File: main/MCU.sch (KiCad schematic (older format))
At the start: 1 part

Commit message: Some cleanup
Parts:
- added C?: 1uF, symbol Device:C
- added C? (x3): 10nF, symbol Device:C
- added C? (x3): 10uF, symbol Device:C
- added C? (x7): 0.1uF, symbol Device:C
- added U?: EFM32GG990F1024, symbol energymicro-efm32:EFM32GG990F1024
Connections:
- new net: C?.1, C?.1, C?.1, C?.1, C?.1, C?.1, C?.1, C?.1, C?.1, U?.D5 (IOVDD_6), U?.F8 (VDD_DREG), U?.G4 (IOVDD_0), U?.K8 (AVDD_2), U?.K9 (AVDD_1), U?.L10 (AVDD_0)
- new net: C?.1, U?.D7 (IOVDD_5)
- new net: C?.1, U?.F11 (DECOUPLE)
- new net: C?.1, U?.G8 (IOVDD_4)
- new net: C?.1, U?.H7 (IOVDD_3)
- new net: C?.1, U?.L4 (IOVDD_1)
- new net GND: C?.2, C?.2, C?.2, C?.2, C?.2, C?.2, C?.2, C?.2, C?.2, C?.2, C?.2, C?.2, C?.2, U?.C7 (VSS), U?.D4 (VSS), U?.G3 (VSS), U?.G9 (VSS), U?.H6 (VSS), U?.K4 (VSS)
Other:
- moved on the sheet: U?C

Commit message: Setup DAC.
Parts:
- gave numbers to parts that had none: 15
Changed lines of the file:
@@
 $Descr A4 11693 8268
 encoding utf-8
-Sheet 2 4
+Sheet 4 5
 Title ""
 Date ""
@@
 VMCU
 $Comp
-L energymicro-efm32:EFM32GG990F1024 U?
+L energymicro-efm32:EFM32GG990F1024 U2
 U 3 1 613D4762
 P 12500 600
-F 0 "U?" H 17718 -697 60  0000 L CNN
+F 0 "U2" H 17718 -697 60  0000 L CNN
 F 1 "EFM32GG990F1024" H 17718 -803 60  0000 L CNN
 F 2 "" H 12500 600 50  0001 C CNN
@@
 	12350 700  12500 700
 $Comp
-L energymicro-efm32:EFM32GG990F1024 U?
+L energymicro-efm32:EFM32GG990F1024 U2
 U 4 1 6138C111
 P 2750 1450
-F 0 "U?" H 3550 1787 60  0000 C CNN
+F 0 "U2" H 3550 1787 60  0000 C CNN
 F 1 "EFM32GG990F1024" H 3550 1681 60  0000 C CNN
 F 2 "" H 2750 1450 50  0001 C CNN
@@
 $EndComp
 $Comp
-L power:GND #PWR?
+L power:GND #PWR012
 U 1 1 61396B35
 P 4550 3950
-F 0 "#PWR?" H 4550 3700 50  0001 C CNN
+F 0 "#PWR012" H 4550 3700 50  0001 C CNN
 F 1 "GND" H 4555 3777 50  0000 C CNN
 F 2 "" H 4550 3950 50  0001 C CNN
@@
 Connection ~ 4550 3450
 $Comp
-L Device:C C?
+L Device:C C11
 U 1 1 61398A68
 P 4700 1600
-F 0 "C?" H 4815 1646 50  0000 L CNN
+F 0 "C11" H 4815 1646 50  0000 L CNN
 F 1 "1uF" H 4815 1555 50  0000 L CNN
 F 2 "" H 4738 1450 50  0001 C CNN
@@
 	4350 1450 4700 1450
 $Comp
-L Device:C C?
+L Device:C C6
 U 1 1 6139B558
 P 1950 2700
-F 0 "C?" H 2065 2746 50  0000 L CNN
+F 0 "C6" H 2065 2746 50  0000 L CNN
 F 1 "10nF" H 2065 2655 50  0000 L CNN
 F 2 "" H 1988 2550 50  0001 C CNN
@@
 $EndComp
 $Comp
-L Device:C C?
+L Device:C C7
 U 1 1 6139B7D9
 P 1950 3300
-F 0 "C?" H 2065 3346 50  0000 L CNN
+F 0 "C7" H 2065 3346 50  0000 L CNN
 F 1 "10nF" H 2065 3255 50  0000 L CNN
 F 2 "" H 1988 3150 50  0001 C CNN
@@
 $EndComp
 $Comp
-L Device:C C?
+L Device:C C8
 U 1 1 6139BBCD
 P 1950 3850
-F 0 "C?" H 2065 3896 50  0000 L CNN
+F 0 "C8" H 2065 3896 50  0000 L CNN
 F 1 "10nF" H 2065 3805 50  0000 L CNN
 F 2 "" H 1988 3700 50  0001 C CNN
@@
 	2450 3700 1950 3700
 $Comp
-L power:GND #PWR?
+L power:GND #PWR08
 U 1 1 6139F150
 P 1950 2850
-F 0 "#PWR?" H 1950 2600 50  0001 C CNN
+F 0 "#PWR08" H 1950 2600 50  0001 C CNN
 F 1 "GND" H 1955 2677 50  0000 C CNN
 F 2 "" H 1950 2850 50  0001 C CNN
@@
 $EndComp
 $Comp
-L power:GND #PWR?
+L power:GND #PWR09
 U 1 1 6139F4DD
 P 1950 3450
-F 0 "#PWR?" H 1950 3200 50  0001 C CNN
+F 0 "#PWR09" H 1950 3200 50  0001 C CNN
 F 1 "GND" H 1955 3277 50  0000 C CNN
 F 2 "" H 1950 3450 50  0001 C CNN
@@
 $EndComp
 $Comp
-L power:GND #PWR?
+L power:GND #PWR010
 U 1 1 6139F8FB
 P 1950 4250
-F 0 "#PWR?" H 1950 4000 50  0001 C CNN
+F 0 "#PWR010" H 1950 4000 50  0001 C CNN
 F 1 "GND" H 1955 4077 50  0000 C CNN
 F 2 "" H 1950 4250 50  0001 C CNN
@@
 	1950 4100 1950 4000
 $Comp
-L Device:C C?
+L Device:C C5
 U 1 1 613A0F20
 P 1600 3850
-F 0 "C?" H 1400 3900 50  0000 L CNN
+F 0 "C5" H 1400 3900 50  0000 L CNN
 F 1 "10uF" H 1300 3800 50  0000 L CNN
 F 2 "" H 1638 3700 50  0001 C CNN
@@
 Connection ~ 1600 2550
 $Comp
-L Device:C C?
+L Device:C C9
 U 1 1 613A45C1
 P 2050 1150
-F 0 "C?" H 2165 1196 50  0000 L CNN
+F 0 "C9" H 2165 1196 50  0000 L CNN
 F 1 "10uF" H 2165 1105 50  0000 L CNN
 F 2 "" H 2088 1000 50  0001 C CNN
@@
 	2050 1000 1600 1000
 $Comp
-L Device:C C?
+L Device:C C10
 U 1 1 613A49A0
 P 2450 1150
-F 0 "C?" H 2565 1196 50  0000 L CNN
+F 0 "C10" H 2565 1196 50  0000 L CNN
 F 1 "0.1uF" H 2565 1105 50  0000 L CNN
 F 2 "" H 2488 1000 50  0001 C CNN
@@
 	2050 1300 2450 1300
 $Comp
-L power:GND #PWR?
+L power:GND #PWR011
 U 1 1 613A5C64
 P 2450 1300
-F 0 "#PWR?" H 2450 1050 50  0001 C CNN
+F 0 "#PWR011" H 2450 1050 50  0001 C CNN
 F 1 "GND" H 2455 1127 50  0000 C CNN
 F 2 "" H 2450 1300 50  0001 C CNN
@@
 Connection ~ 1600 1000
 $Comp
-L Device:C C?
+L Device:C C12
 U 1 1 613D0172
 P 5600 2400
-F 0 "C?" H 5715 2446 50  0000 L CNN
+F 0 "C12" H 5715 2446 50  0000 L CNN
 F 1 "0.1uF" H 5715 2355 50  0000 L CNN
 F 2 "" H 5638 2250 50  0001 C CNN
@@
 $EndComp
 $Comp
-L power:GND #PWR?
+L power:GND #PWR013
 U 1 1 613D08CB
 P 5600 2550
-F 0 "#PWR?" H 5600 2300 50  0001 C CNN
+F 0 "#PWR013" H 5600 2300 50  0001 C CNN
 F 1 "GND" H 5605 2377 50  0000 C CNN
 F 2 "" H 5600 2550 50  0001 C CNN
@@
 $EndComp
 $Comp
-L Device:C C?
+L Device:C C13
 U 1 1 613D1833
 P 5600 3000
-F 0 "C?" H 5715 3046 50  0000 L CNN
+F 0 "C13" H 5715 3046 50  0000 L CNN
 F 1 "0.1uF" H 5715 2955 50  0000 L CNN
 F 2 "" H 5638 2850 50  0001 C CNN
@@
 $EndComp
 $Comp
-L power:GND #PWR?
+L power:GND #PWR014
 U 1 1 613D1839
 P 5600 3150
-F 0 "#PWR?" H 5600 2900 50  0001 C CNN
+F 0 "#PWR014" H 5600 2900 50  0001 C CNN
 F 1 "GND" H 5605 2977 50  0000 C CNN
 F 2 "" H 5600 3150 50  0001 C CNN
@@
 $EndComp
 $Comp
-L Device:C C?
+L Device:C C14
 U 1 1 613D2781
 P 5600 3600
-F 0 "C?" H 5715 3646 50  0000 L CNN
+F 0 "C14" H 5715 3646 50  0000 L CNN
 F 1 "0.1uF" H 5715 3555 50  0000 L CNN
 F 2 "" H 5638 3450 50  0001 C CNN
@@
 $EndComp
 $Comp
-L power:GND #PWR?
+L power:GND #PWR015
 U 1 1 613D2787
 P 5600 3750
-F 0 "#PWR?" H 5600 3500 50  0001 C CNN
+F 0 "#PWR015" H 5600 3500 50  0001 C CNN
 F 1 "GND" H 5605 3577 50  0000 C CNN
 F 2 "" H 5600 3750 50  0001 C CNN
@@
 	5400 3450 5600 3450
 $Comp
-L Device:C C?
+L Device:C C15
 U 1 1 613E0C7C
 P 5600 4150
-F 0 "C?" H 5715 4196 50  0000 L CNN
+F 0 "C15" H 5715 4196 50  0000 L CNN
 F 1 "0.1uF" H 5715 4105 50  0000 L CNN
 F 2 "" H 5638 4000 50  0001 C CNN
@@
 $EndComp
 $Comp
-L power:GND #PWR?
+L power:GND #PWR016
 U 1 1 613E0C82
 P 5600 4300
-F 0 "#PWR?" H 5600 4050 50  0001 C CNN
+F 0 "#PWR016" H 5600 4050 50  0001 C CNN
 F 1 "GND" H 5605 4127 50  0000 C CNN
 F 2 "" H 5600 4300 50  0001 C CNN
@@
 $EndComp
 $Comp
-L Device:C C?
+L Device:C C16
 U 1 1 613E0C88
 P 5600 4750
-F 0 "C?" H 5715 4796 50  0000 L CNN
+F 0 "C16" H 5715 4796 50  0000 L CNN
 F 1 "0.1uF" H 5715 4705 50  0000 L CNN
 F 2 "" H 5638 4600 50  0001 C CNN
@@
 $EndComp
 $Comp
-L power:GND #PWR?
+L power:GND #PWR017
 U 1 1 613E0C8E
 P 5600 4900
-F 0 "#PWR?" H 5600 4650 50  0001 C CNN
+F 0 "#PWR017" H 5600 4650 50  0001 C CNN
 F 1 "GND" H 5605 4727 50  0000 C CNN
 F 2 "" H 5600 4900 50  0001 C CNN
@@
 	5250 2750 5250 5200
 $Comp
-L power:GND #PWR?
+L power:GND #PWR018
 U 1 1 613E0C9A
 P 6100 5500
-F 0 "#PWR?" H 6100 5250 50  0001 C CNN
+F 0 "#PWR018" H 6100 5250 50  0001 C CNN
 F 1 "GND" H 6105 5327 50  0000 C CNN
 F 2 "" H 6100 5500 50  0001 C CNN
@@
 	5250 5200 5600 5200
 $Comp
-L Device:C C?
+L Device:C C17
 U 1 1 613E0C94
 P 5600 5350
-F 0 "C?" H 5715 5396 50  0000 L CNN
+F 0 "C17" H 5715 5396 50  0000 L CNN
 F 1 "0.1uF" H 5715 5305 50  0000 L CNN
 F 2 "" H 5638 5200 50  0001 C CNN
@@
 	5600 5500 6100 5500
 $Comp
-L Device:C C?
+L Device:C C18
 U 1 1 613E8B65
 P 6100 5350
-F 0 "C?" H 6215 5396 50  0000 L CNN
+F 0 "C18" H 6215 5396 50  0000 L CNN
 F 1 "10uF" H 6215 5305 50  0000 L CNN
 F 2 "" H 6138 5200 50  0001 C CNN
@@
 Wire Wire Line
 	6100 2250 5600 2250
+Entry Wire Line
+	7700 4000 7800 4100
+Entry Wire Line
+	7700 3850 7800 3950
+Entry Wire Line
+	7700 3700 7800 3800
+Entry Wire Line
+	7700 3550 7800 3650
+Text HLabel 8250 4100 2    50   Input ~ 0
+~MCU_SPI_PS
+Text HLabel 8250 3950 2    50   Output ~ 0
+MCU_SPI_CIPO
+Text HLabel 8250 3800 2    50   Input ~ 0
+MCU_SPI_COPI
+Text HLabel 8250 3650 2    50   Input ~ 0
+MCU_SPI_PCLK
+Text Label 7700 3350 0    50   ~ 0
+FPGA_SPI[0..3]
+Text Label 7800 3950 0    50   ~ 0
+FPGA_SPI2
+Text Label 7800 4100 0    50   ~ 0
+FPGA_SPI3
+Wire Wire Line
+	7800 3650 8250 3650
+Wire Wire Line
+	7800 3800 8250 3800
+Wire Wire Line
+	7800 3950 8250 3950
+Wire Wire Line
+	7800 4100 8250 4100
+Wire Bus Line
+	7700 3300 7550 3300
+Text HLabel 7550 3300 0    50   BiDi ~ 0
+FPGA_SPI
+Wire Bus Line
+	7700 3300 7700 4000
+Text Label 7800 3650 0    50   ~ 0
+FPGA_SPI0
+Text Label 7800 3800 0    50   ~ 0
+FPGA_SPI1
 $EndSCHEMATC

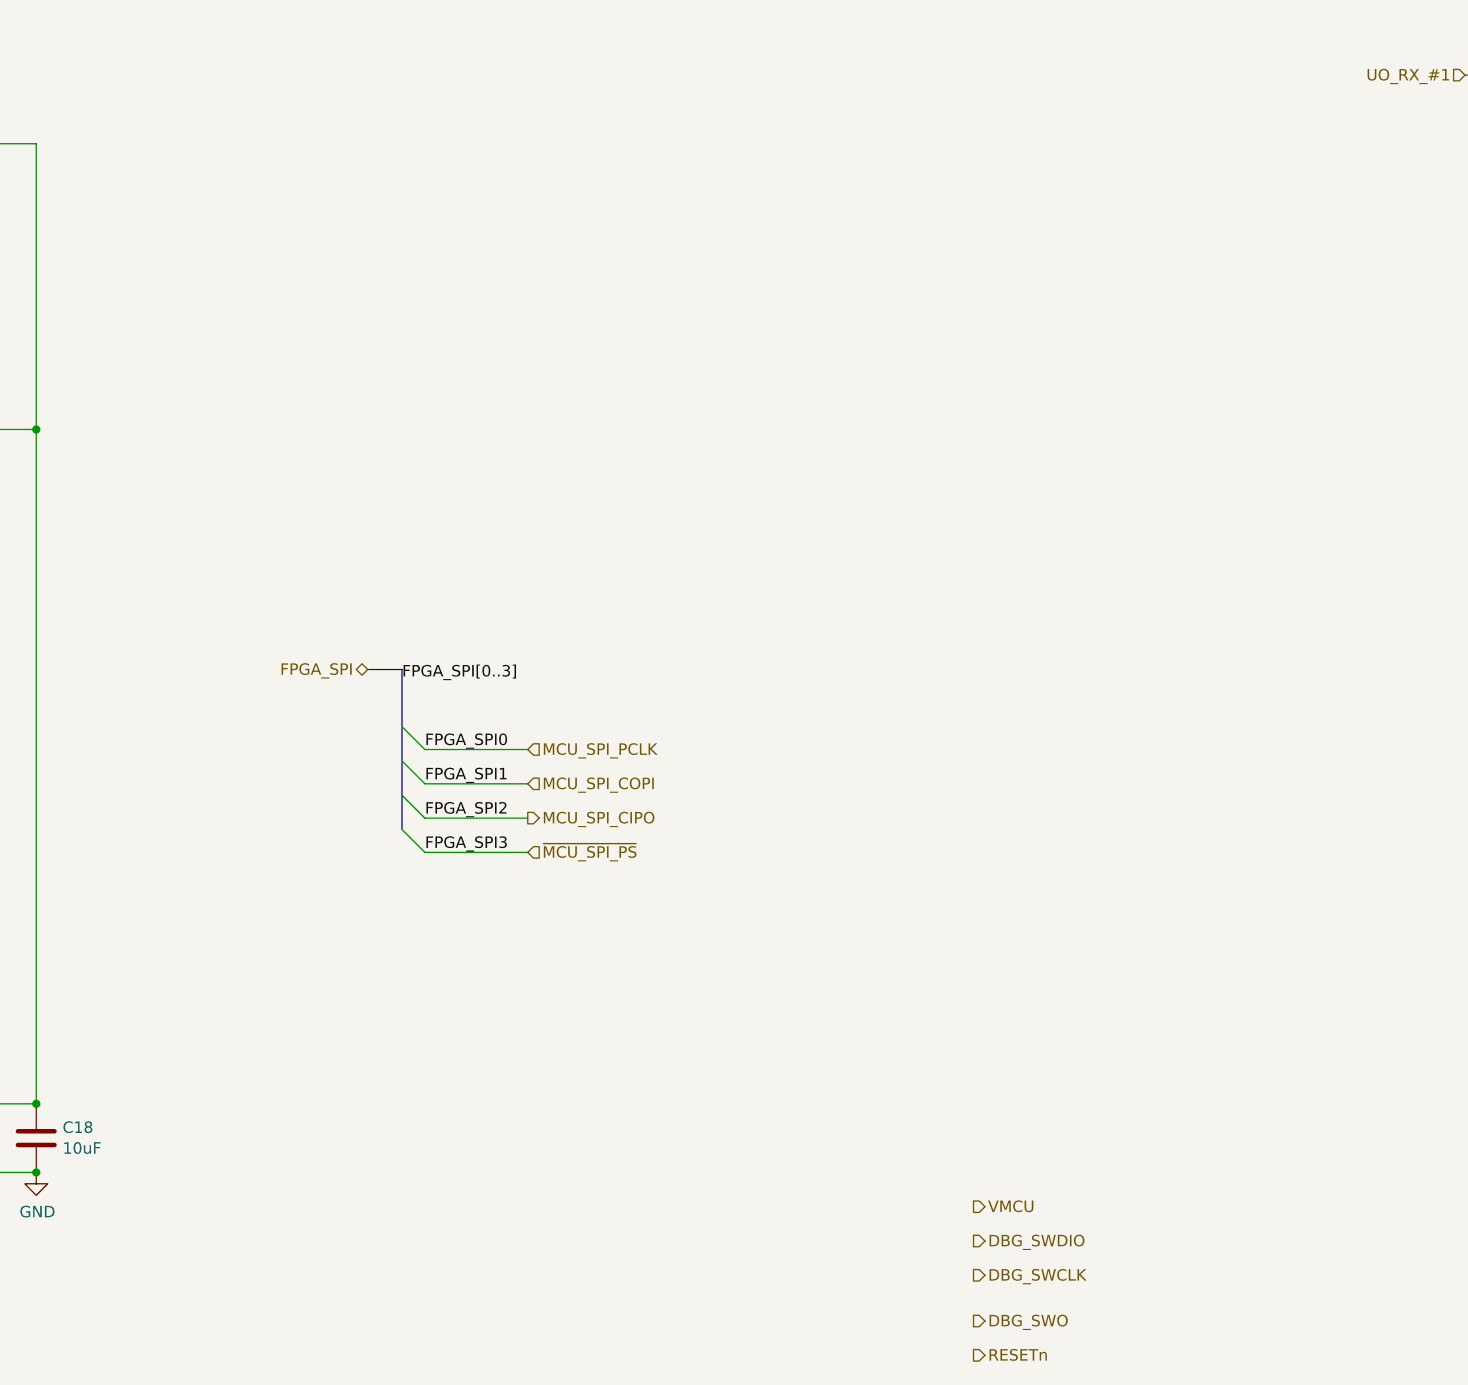
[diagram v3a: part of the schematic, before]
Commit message: Move EFM32GG debug port inside MCU sheet
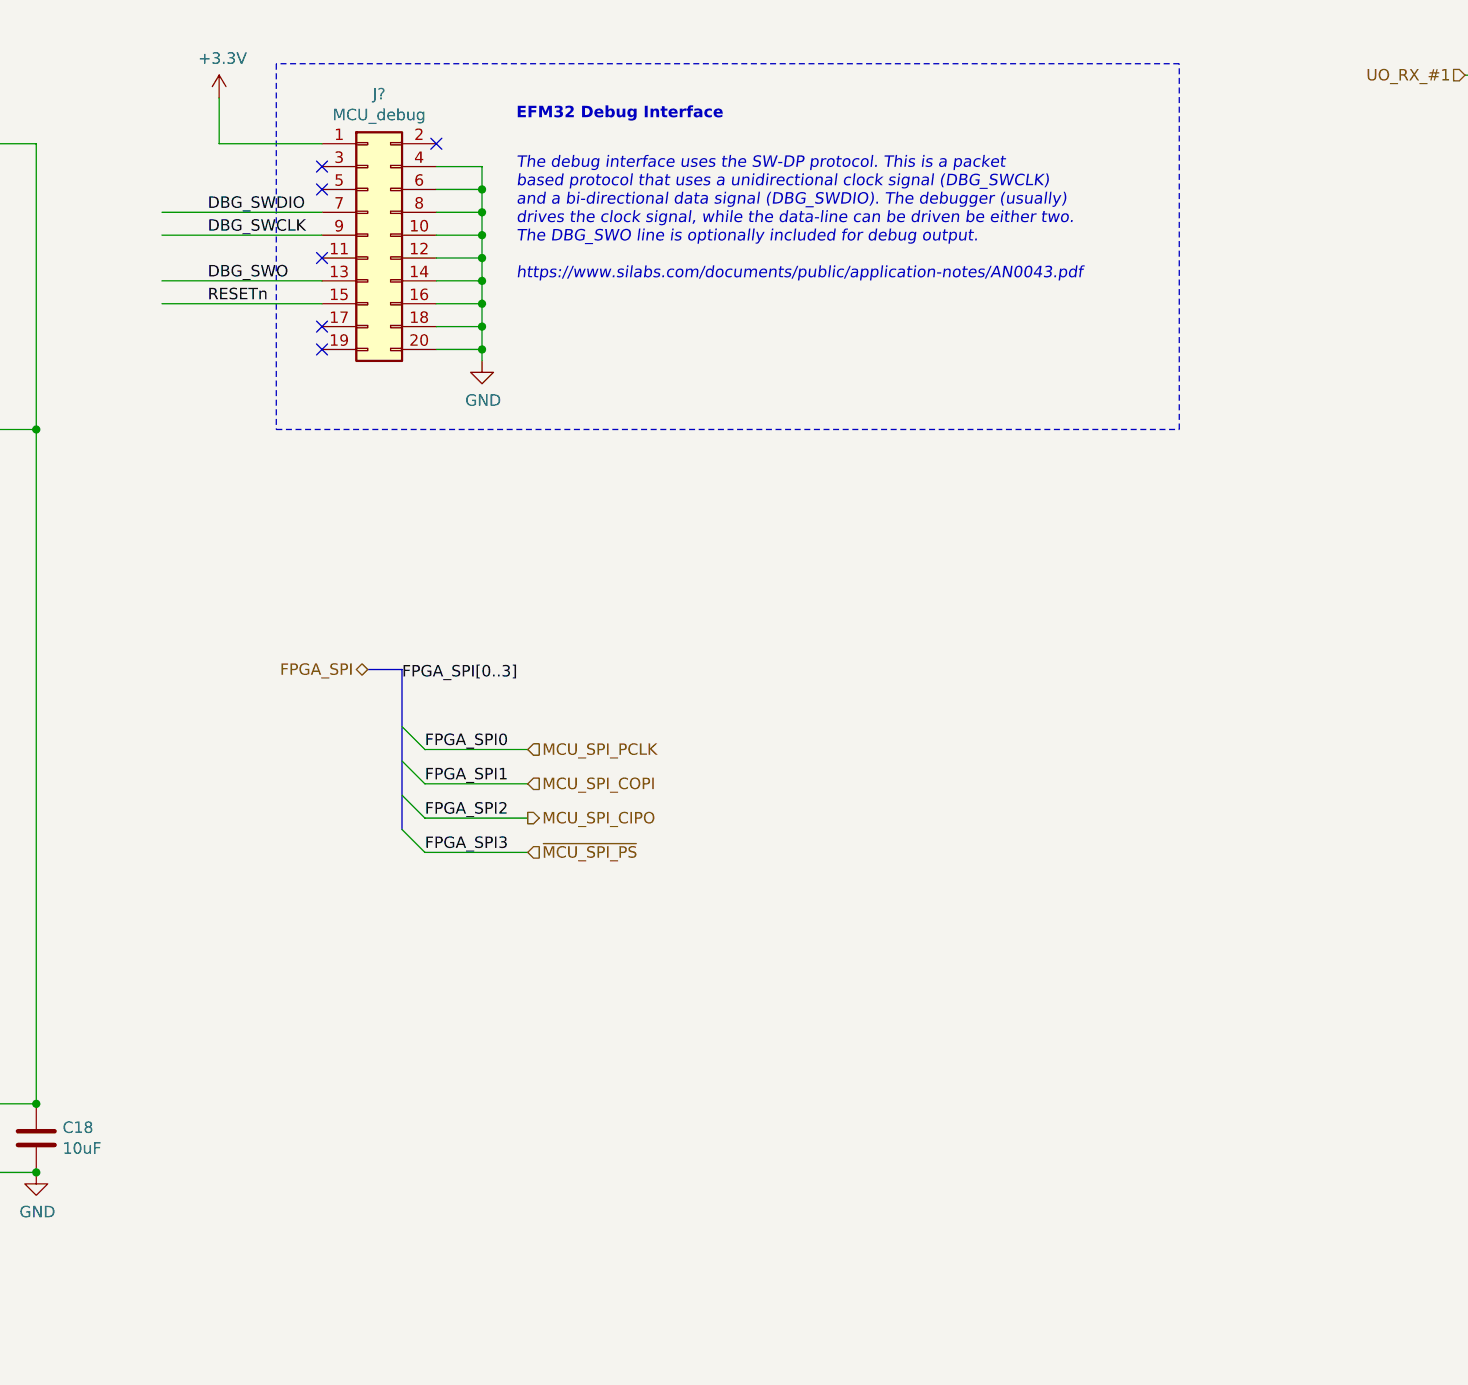
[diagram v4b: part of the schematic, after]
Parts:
- added J?: MCU_debug, symbol Connector_Generic:Conn_02x10_Odd_Even
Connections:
- net labels added: +3.3V
- net labels removed: VMCU
- wire segments 64 -> 88
- no-connect marks 0 -> 6
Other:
- note added: "EFM32 Debug Interface"
- note added: "The debug interface uses the SW-DP protocol. This is a packet \nbased protocol that uses a unidirectional clock signal (DBG_SWCLK) \nand a bi-directional data signal (DBG_SWDIO). The debugger (usually)\ndrives the clock signal, while the data-line can be driven be either two.\nThe DBG_SWO line is optionally included for debug output.\n\nhttps://www.silabs.com/documents/public/application-notes/AN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"
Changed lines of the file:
@@
 $Descr A4 11693 8268
 encoding utf-8
-Sheet 4 5
+Sheet 5 5
 Title ""
 Date ""
@@
 Comment4 ""
 $EndDescr
-Text HLabel 10200 5800 2    50   Output ~ 0
-DBG_SWDIO
-Text HLabel 10200 5950 2    50   Output ~ 0
-DBG_SWCLK
-Text HLabel 10200 6150 2    50   Output ~ 0
-DBG_SWO
-Text HLabel 10200 6300 2    50   Output ~ 0
-RESETn
-Text HLabel 10200 5650 2    50   Output ~ 0
-VMCU
 $Comp
 L energymicro-efm32:EFM32GG990F1024 U2
@@
 Text HLabel 7550 3300 0    50   BiDi ~ 0
 FPGA_SPI
-Wire Bus Line
-	7700 3300 7700 4000
 Text Label 7800 3650 0    50   ~ 0
 FPGA_SPI0
 Text Label 7800 3800 0    50   ~ 0
 FPGA_SPI1
+Wire Notes Line
+	11100 650  7150 650
+Text Notes 8200 1600 0    50   Italic 0
+The debug interface uses the SW-DP protocol. This is a packet \nbased protocol that uses a unidirectional clock signal (DBG_SWCLK) \nand a bi-directional data signal (DBG_SWDIO). The debugger (usually)\ndrives the clock signal, while the data-line can be driven be either two.\nThe DBG_SWO line is optionally included for debug output.\n\nhttps://www.silabs.com/documents/public/application-notes/AN0043.pdf
+NoConn ~ 7350 1900
+NoConn ~ 7350 1800
+Wire Wire Line
+	8050 1200 8050 1300
+Connection ~ 8050 1200
+Wire Wire Line
+	8050 1100 8050 1200
+Wire Wire Line
+	7850 1100 8050 1100
+Connection ~ 8050 1300
+Wire Wire Line
+	7850 1200 8050 1200
+Wire Wire Line
+	8050 1400 8050 1500
+Connection ~ 8050 1400
+Wire Wire Line
+	8050 1300 8050 1400
+Wire Wire Line
+	7850 1300 8050 1300
+Connection ~ 8050 1500
+Wire Wire Line
+	7850 1400 8050 1400
+Wire Wire Line
+	8050 1600 8050 1700
+Connection ~ 8050 1600
+Wire Wire Line
+	8050 1500 8050 1600
+Wire Wire Line
+	7850 1500 8050 1500
+Wire Wire Line
+	8050 1700 8050 1800
+Connection ~ 8050 1700
+Wire Wire Line
+	7850 1600 8050 1600
+Connection ~ 8050 1800
+Wire Wire Line
+	7850 1700 8050 1700
+Wire Wire Line
+	8050 1900 8050 1950
+Connection ~ 8050 1900
+Wire Wire Line
+	8050 1800 8050 1900
+Wire Wire Line
+	7850 1800 8050 1800
+Wire Wire Line
+	7850 1900 8050 1900
+$Comp
+L power:GND #PWR?
+U 1 1 614132A5
+P 8050 1950
+AR Path="/614132A5" Ref="#PWR?"  Part="1"
+AR Path="/6139E7E0/614132A5" Ref="#PWR?"  Part="1"
+F 0 "#PWR?" H 8050 1700 50  0001 C CNN
+F 1 "GND" H 8055 1777 50  0000 C CNN
+F 2 "" H 8050 1950 50  0001 C CNN
+F 3 "" H 8050 1950 50  0001 C CNN
+	1    8050 1950
+	1    0    0    -1
+$EndComp
+NoConn ~ 7350 1500
+NoConn ~ 7350 1200
+NoConn ~ 7350 1100
+NoConn ~ 7850 1000
+$Comp
+L Connector_Generic:Conn_02x10_Odd_Even J?
+U 1 1 614132AF
+P 7550 1400
+AR Path="/614132AF" Ref="J?"  Part="1"
+AR Path="/6139E7E0/614132AF" Ref="J?"  Part="1"
+F 0 "J?" H 7600 2017 50  0000 C CNN
+F 1 "MCU_debug" H 7600 1926 50  0000 C CNN
+F 2 "" H 7550 1400 50  0001 C CNN
+F 3 "~" H 7550 1400 50  0001 C CNN
+	1    7550 1400
+	1    0    0    -1
+$EndComp
+Text Notes 8200 900  0    50   ~ 10
+EFM32 Debug Interface
+Wire Notes Line
+	7150 650  7150 2250
+Wire Notes Line
+	11100 2250 11100 650
+Wire Notes Line
+	7150 2250 11100 2250
+Wire Wire Line
+	6650 1300 7350 1300
+Wire Wire Line
+	6650 1600 7350 1600
+Wire Wire Line
+	6650 1700 7350 1700
+Wire Wire Line
+	6650 1400 7350 1400
+Text Label 6850 1300 0    50   ~ 0
+DBG_SWDIO
+Text Label 6850 1400 0    50   ~ 0
+DBG_SWCLK
+Text Label 6850 1600 0    50   ~ 0
+DBG_SWO
+Text Label 6850 1700 0    50   ~ 0
+RESETn
+$Comp
+L power:+3.3V #PWR?
+U 1 1 61424886
+P 6900 800
+F 0 "#PWR?" H 6900 650 50  0001 C CNN
+F 1 "+3.3V" H 6915 973 50  0000 C CNN
+F 2 "" H 6900 800 50  0001 C CNN
+F 3 "" H 6900 800 50  0001 C CNN
+	1    6900 800
+	1    0    0    -1
+$EndComp
+Wire Wire Line
+	6900 800  6900 1000
+Wire Wire Line
+	6900 1000 7350 1000
+Wire Bus Line
+	7700 3300 7700 4000
 $EndSCHEMATC
